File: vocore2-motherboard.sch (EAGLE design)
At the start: 106 parts, among them IC1 AP63205, IC2 FE1.1S, IC3 LM3671MF-3.3, IC4 LM3671MF-3.3, IC5 LM3671MF-3.3, IC7 742G17DBV, IC8 FT230XS-R, J1 RJHSE-5381, J2 TE_1775470-8, J3 AMPHENOL_1140084168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

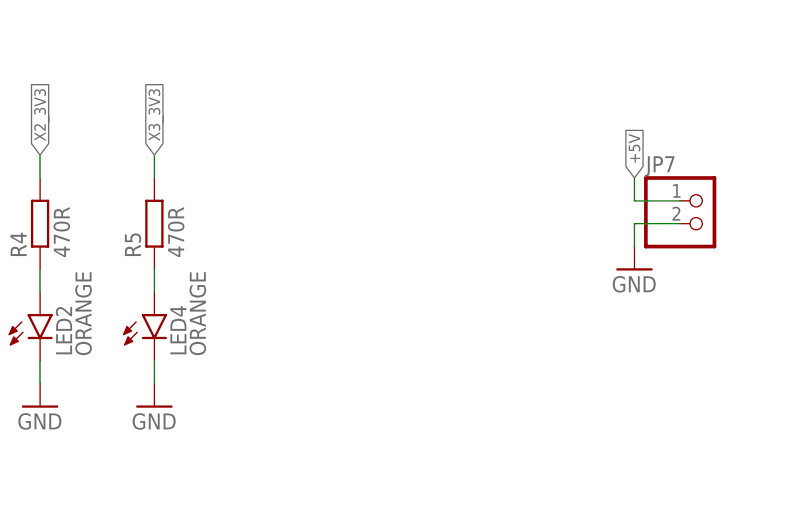
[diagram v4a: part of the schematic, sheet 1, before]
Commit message: feat: network led breakout
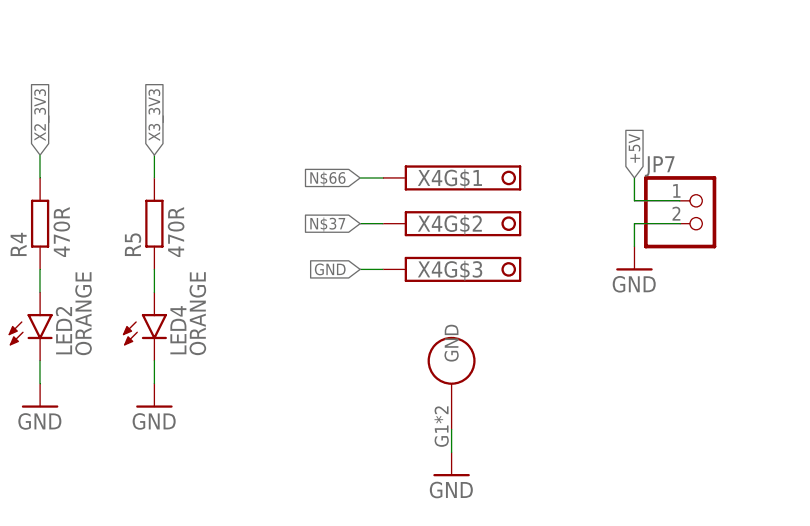
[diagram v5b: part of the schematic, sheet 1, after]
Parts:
- added X4: BM03B-SRSS-TB, con-jst:BM03B-SRSS-TB
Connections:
- net GND: now also X4G$3.K, X4G$4.GND
- net N$37: now also X4G$2.K
- net N$66: now also X4G$1.K
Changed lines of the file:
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@@
 <attribute name="SPICEPREFIX" value="G"/>
 </part>
+<part name="X4" library="con-jst" deviceset="BM03B-SRSS-TB" device=""/>
+<part name="GND50" library="supply1" deviceset="GND" device=""/>
 </parts>
 <sheets>
@@
 <attribute name="VALUE" x="236.22" y="40.64" size="1.778" layer="96"/>
 </instance>
+<instance part="X4" gate="G$1" x="109.22" y="45.72" smashed="yes">
+<attribute name="NAME" x="110.49" y="44.831" size="1.778" layer="95"/>
+</instance>
+<instance part="X4" gate="G$2" x="109.22" y="40.64" smashed="yes">
+<attribute name="NAME" x="110.49" y="39.751" size="1.778" layer="95"/>
+</instance>
+<instance part="X4" gate="G$3" x="109.22" y="35.56" smashed="yes">
+<attribute name="NAME" x="110.49" y="34.671" size="1.778" layer="95"/>
+</instance>
+<instance part="X4" gate="G$4" x="114.3" y="22.86" smashed="yes"/>
+<instance part="GND50" gate="1" x="114.3" y="12.7" smashed="yes">
+<attribute name="VALUE" x="111.76" y="10.16" size="1.778" layer="96"/>
+</instance>
 </instances>
 <busses>
@@
 <wire x1="238.76" y1="48.26" x2="238.76" y2="45.72" width="0.1524" layer="91"/>
 <pinref part="GND46" gate="1" pin="GND"/>
+</segment>
+<segment>
+<pinref part="X4" gate="G$4" pin="GND"/>
+<wire x1="114.3" y1="17.78" x2="114.3" y2="15.24" width="0.1524" layer="91"/>
+<pinref part="GND50" gate="1" pin="GND"/>
+</segment>
+<segment>
+<pinref part="X4" gate="G$3" pin="K"/>
+<wire x1="106.68" y1="35.56" x2="104.14" y2="35.56" width="0.1524" layer="91"/>
+<label x="104.14" y="35.56" size="1.27" layer="95" rot="R180" xref="yes"/>
 </segment>
 </net>
@@
 </segment>
 </net>
+<net name="N$37" class="0">
+<segment>
+<pinref part="X4" gate="G$2" pin="K"/>
+<wire x1="106.68" y1="40.64" x2="104.14" y2="40.64" width="0.1524" layer="91"/>
+<label x="104.14" y="40.64" size="1.27" layer="95" rot="R180" xref="yes"/>
+</segment>
+</net>
+<net name="N$66" class="0">
+<segment>
+<pinref part="X4" gate="G$1" pin="K"/>
+<wire x1="106.68" y1="45.72" x2="104.14" y2="45.72" width="0.1524" layer="91"/>
+<label x="104.14" y="45.72" size="1.27" layer="95" rot="R180" xref="yes"/>
+</segment>
+</net>

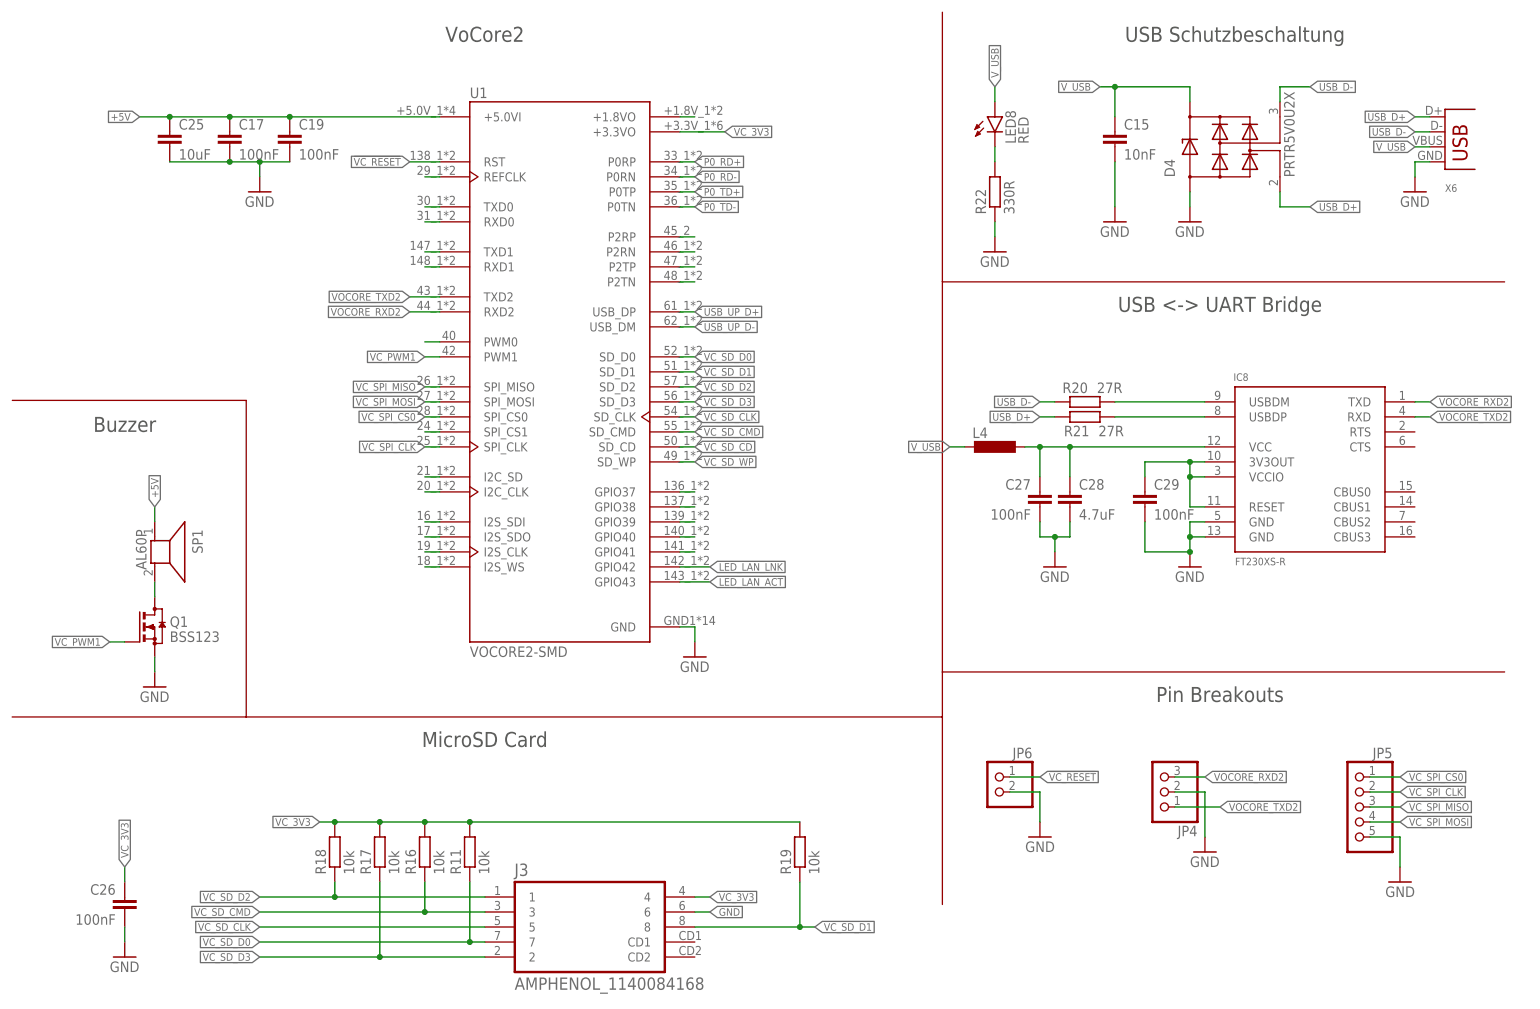
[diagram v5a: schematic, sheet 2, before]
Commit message: feat(pcb): removed through-hole mounts for vocore2
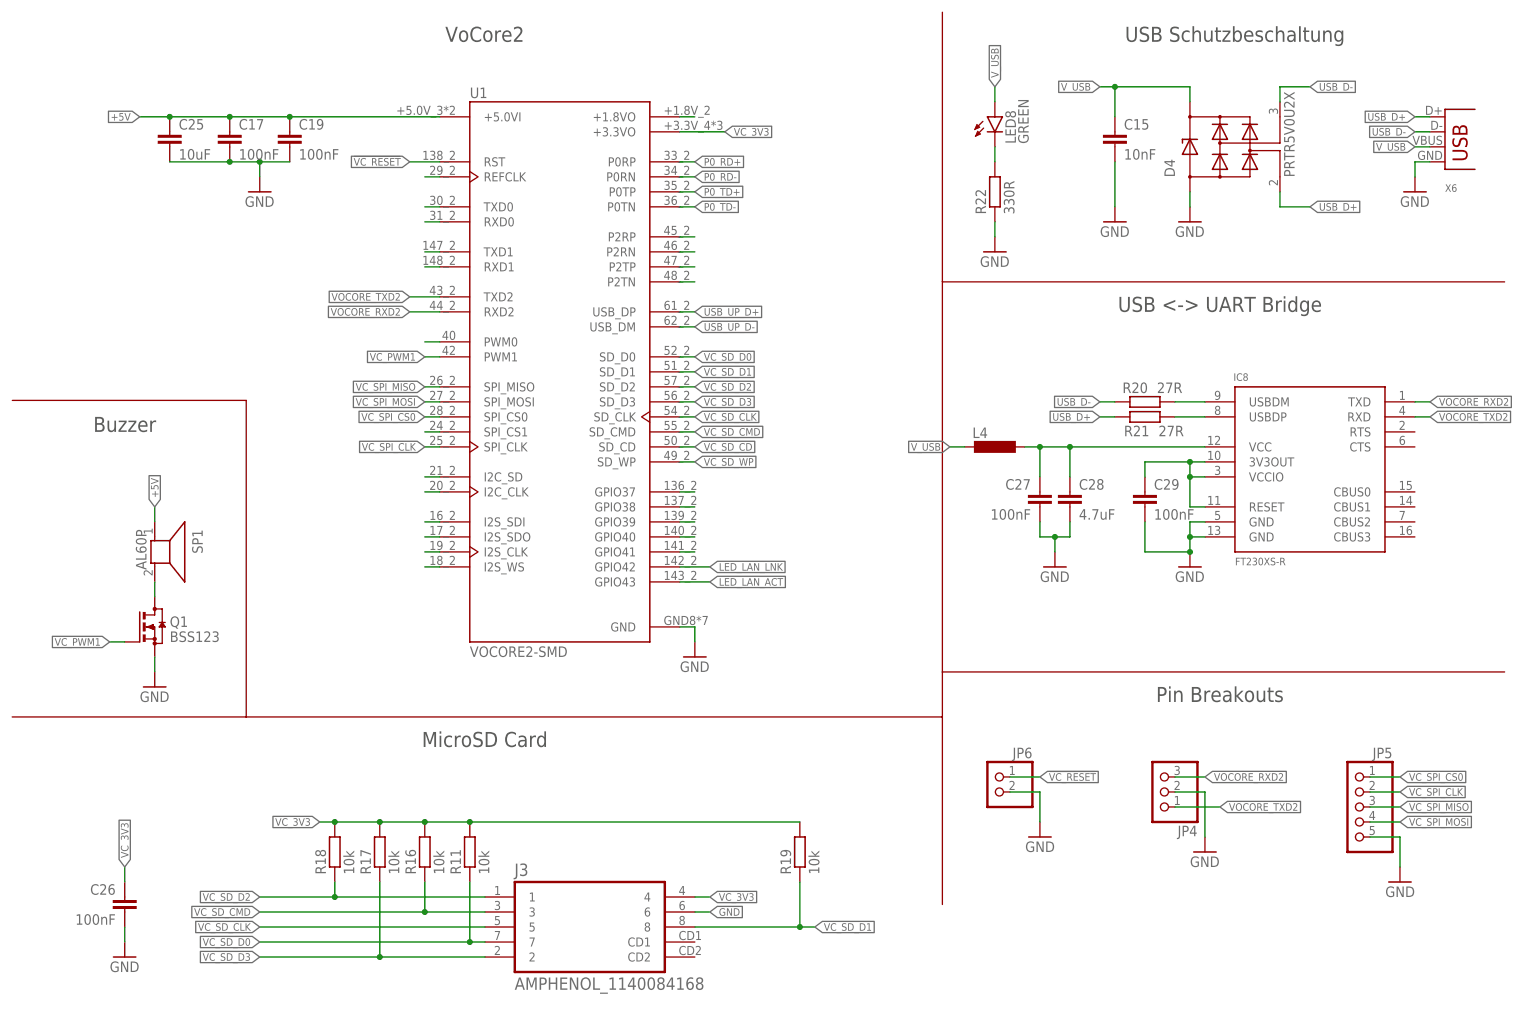
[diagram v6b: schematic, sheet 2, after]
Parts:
- C18: BUERKLIN 53 D 3425 -> (none); DIGIKEY (none) -> 587-2994-1-ND; MBM 10 -> (none); PREIS 0,61 -> (none)
- C57: BUERKLIN 56D510 -> (none); DIGIKEY (none) -> 709-1021-1-ND; MBM 1 -> (none); PREIS 0,13 -> (none)
- LED8: value RED -> GREEN; DIGIKEY 160-1447-1-ND -> 160-1446-1-ND
- R3: value 330R -> 470R
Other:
- note added: "I=6.4mA @ Vf=2V"
- note removed: "I=10mA @ Vf=2V"
- moved on the sheet: R20, R21
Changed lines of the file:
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@@
 </part>
 <part name="C18" library="rcl" deviceset="C-EU" device="C1206" value="4.7µF 50V">
-<attribute name="BUERKLIN" value="53 D 3425"/>
-<attribute name="MBM" value="10"/>
-<attribute name="PREIS" value="0,61"/>
+<attribute name="DIGIKEY" value="587-2994-1-ND"/>
 </part>
 <part name="D3" library="diode" library_urn="urn:adsk.eagle:library:210" deviceset="DIODE-" device="SMB" package3d_urn="urn:adsk.eagle:package:43404/2">
@@
 </part>
 <part name="GND9" library="supply1" deviceset="GND" device=""/>
-<part name="R3" library="rcl" library_urn="urn:adsk.eagle:library:334" deviceset="R-EU_" device="R0603" package3d_urn="urn:adsk.eagle:package:23555/3" value="330R"/>
+<part name="R3" library="rcl" library_urn="urn:adsk.eagle:library:334" deviceset="R-EU_" device="R0603" package3d_urn="urn:adsk.eagle:package:23555/3" value="470R"/>
 <part name="IC4" library="texas" library_urn="urn:adsk.eagle:library:387" deviceset="LM3671" device="" value="LM3671MF-3.3">
 <attribute name="DIGIKEY" value="LM3671MF-3.3/NOPBCT-ND"/>
@@
 <part name="GND34" library="supply1" deviceset="GND" device=""/>
 <part name="C57" library="rcl" deviceset="C-EU" device="C0805" value="10nF 500V">
-<attribute name="BUERKLIN" value="56D510"/>
-<attribute name="MBM" value="1"/>
-<attribute name="PREIS" value="0,13"/>
+<attribute name="DIGIKEY" value="709-1021-1-ND"/>
 </part>
 <part name="GND75" library="supply1" deviceset="GND" device=""/>
@@
 <attribute name="DIGIKEY" value="490-4780-1-ND"/>
 </part>
-<part name="LED8" library="led" library_urn="urn:adsk.eagle:library:259" deviceset="LED" device="CHIP-LED0805" package3d_urn="urn:adsk.eagle:package:15818/2" value="RED">
-<attribute name="DIGIKEY" value="160-1447-1-ND"/>
+<part name="LED8" library="led" library_urn="urn:adsk.eagle:library:259" deviceset="LED" device="CHIP-LED0805" package3d_urn="urn:adsk.eagle:package:15818/2" value="GREEN">
+<attribute name="DIGIKEY" value="160-1446-1-ND"/>
 </part>
 <part name="GND29" library="supply1" deviceset="GND" device=""/>
@@
 <text x="114.3" y="101.6" size="1.27" layer="98" align="bottom-center">2A Continuous
 Output</text>
-<text x="22.86" y="25.4" size="1.778" layer="98" rot="R90">I=10mA @ Vf=2V</text>
+<text x="22.86" y="25.4" size="1.778" layer="98" rot="R90">I=6.4mA @ Vf=2V</text>
 <text x="50.8" y="25.4" size="1.778" layer="98" rot="R90">I=3mA @ Vf=2V</text>
 </plain>
@@
 </instance>
 <instance part="C18" gate="G$1" x="88.9" y="149.86" smashed="yes">
-<attribute name="BUERKLIN" x="88.9" y="149.86" size="1.778" layer="96" display="off"/>
-<attribute name="MBM" x="88.9" y="149.86" size="1.778" layer="96" display="off"/>
-<attribute name="PREIS" x="88.9" y="149.86" size="1.778" layer="96" display="off"/>
 <attribute name="NAME" x="90.424" y="150.241" size="1.778" layer="95"/>
 <attribute name="VALUE" x="90.424" y="145.161" size="1.778" layer="96"/>
+<attribute name="DIGIKEY" x="88.9" y="149.86" size="1.778" layer="96" display="off"/>
 </instance>
 <instance part="D3" gate="G$1" x="38.1" y="154.94" smashed="yes">
@@
 <attribute name="VALUE" x="197.104" y="89.281" size="1.778" layer="96"/>
 </instance>
-<instance part="R20" gate="G$1" x="185.42" y="109.22" smashed="yes">
-<attribute name="NAME" x="181.61" y="110.7186" size="1.778" layer="95"/>
-<attribute name="VALUE" x="187.452" y="110.7186" size="1.778" layer="96"/>
-</instance>
-<instance part="R21" gate="G$1" x="185.42" y="106.68" smashed="yes" rot="R180">
-<attribute name="NAME" x="186.182" y="105.1814" size="1.778" layer="95" rot="R180"/>
-<attribute name="VALUE" x="192.024" y="105.1814" size="1.778" layer="96" rot="R180"/>
+<instance part="R20" gate="G$1" x="195.58" y="109.22" smashed="yes">
+<attribute name="NAME" x="191.77" y="110.7186" size="1.778" layer="95"/>
+<attribute name="VALUE" x="197.612" y="110.7186" size="1.778" layer="96"/>
+</instance>
+<instance part="R21" gate="G$1" x="195.58" y="106.68" smashed="yes" rot="R180">
+<attribute name="NAME" x="196.342" y="105.1814" size="1.778" layer="95" rot="R180"/>
+<attribute name="VALUE" x="202.184" y="105.1814" size="1.778" layer="96" rot="R180"/>
 </instance>
 <instance part="LED8" gate="G$1" x="170.18" y="157.48" smashed="yes">
@@
 <segment>
 <pinref part="R21" gate="G$1" pin="2"/>
-<wire x1="180.34" y1="106.68" x2="177.8" y2="106.68" width="0.1524" layer="91"/>
-<label x="177.8" y="106.68" size="1.27" layer="95" rot="R180" xref="yes"/>
+<wire x1="190.5" y1="106.68" x2="187.96" y2="106.68" width="0.1524" layer="91"/>
+<label x="187.96" y="106.68" size="1.27" layer="95" rot="R180" xref="yes"/>
 </segment>
 </net>
@@
 <segment>
 <pinref part="R20" gate="G$1" pin="1"/>
-<wire x1="180.34" y1="109.22" x2="177.8" y2="109.22" width="0.1524" layer="91"/>
-<label x="177.8" y="109.22" size="1.27" layer="95" rot="R180" xref="yes"/>
+<wire x1="190.5" y1="109.22" x2="187.96" y2="109.22" width="0.1524" layer="91"/>
+<label x="187.96" y="109.22" size="1.27" layer="95" rot="R180" xref="yes"/>
 </segment>
 </net>
@@
 <pinref part="IC8" gate="G$1" pin="USBDM"/>
 <pinref part="R20" gate="G$1" pin="2"/>
-<wire x1="205.74" y1="109.22" x2="190.5" y2="109.22" width="0.1524" layer="91"/>
+<wire x1="205.74" y1="109.22" x2="200.66" y2="109.22" width="0.1524" layer="91"/>
 </segment>
 </net>
@@
 <pinref part="IC8" gate="G$1" pin="USBDP"/>
 <pinref part="R21" gate="G$1" pin="1"/>
-<wire x1="205.74" y1="106.68" x2="190.5" y2="106.68" width="0.1524" layer="91"/>
+<wire x1="205.74" y1="106.68" x2="200.66" y2="106.68" width="0.1524" layer="91"/>
 </segment>
 </net>
@@
 </instance>
 <instance part="C57" gate="G$1" x="195.58" y="83.82" smashed="yes" rot="MR0">
-<attribute name="BUERKLIN" x="195.58" y="83.82" size="1.778" layer="96" rot="MR0" display="off"/>
-<attribute name="MBM" x="195.58" y="83.82" size="1.778" layer="96" rot="MR0" display="off"/>
-<attribute name="PREIS" x="195.58" y="83.82" size="1.778" layer="96" rot="MR0" display="off"/>
 <attribute name="NAME" x="194.056" y="84.201" size="1.778" layer="95" rot="MR0"/>
 <attribute name="VALUE" x="194.056" y="79.121" size="1.778" layer="96" rot="MR0"/>
+<attribute name="DIGIKEY" x="195.58" y="83.82" size="1.778" layer="96" rot="MR0" display="off"/>
 </instance>
 <instance part="GND75" gate="1" x="195.58" y="73.66" smashed="yes">
